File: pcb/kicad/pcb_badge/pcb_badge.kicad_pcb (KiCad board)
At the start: 2 copper layers, 82 x 132 mm, 249 parts, among them J1 DEALON USB-TYPE-C-018, J2 Conn_01x02_Pin, J3 Conn_01x04_Pin, J4 Conn_01x03_Pin, J5 Conn_01x03_Pin, J7 Conn_01x02_Pin, Q1 SI2302, Q2 JSM2301S, Q9 2N7002, Q90 2N7002, Q91 2N7002, Q910 2N7002, Q911 2N7002, Q912 2N7002, Q913 2N7002, Q914 2N7002, Q915 2N7002, Q92 2N7002, Q93 2N7002, Q94 2N7002, Q95 2N7002, Q96 2N7002, Q97 2N7002, Q98 2N7002, Q99 2N7002, SW1 SW_MEC_5E, SW2 SW_MEC_5E, SW3 SW_MEC_5E, SW4 SW_MEC_5E, SW5 SW_MEC_5E, SW6 SW_MEC_5E, SW7 SW_MEC_5E, SW8 SW_MEC_5E, U1 TLV70328DBVR, U2 QX2304L33F, U3 STM32F103CBT6, U4 74HC238, U6 IRM-H638T/TR2, U8 74HC238, Y1 TAXM8M4RFDCET2T

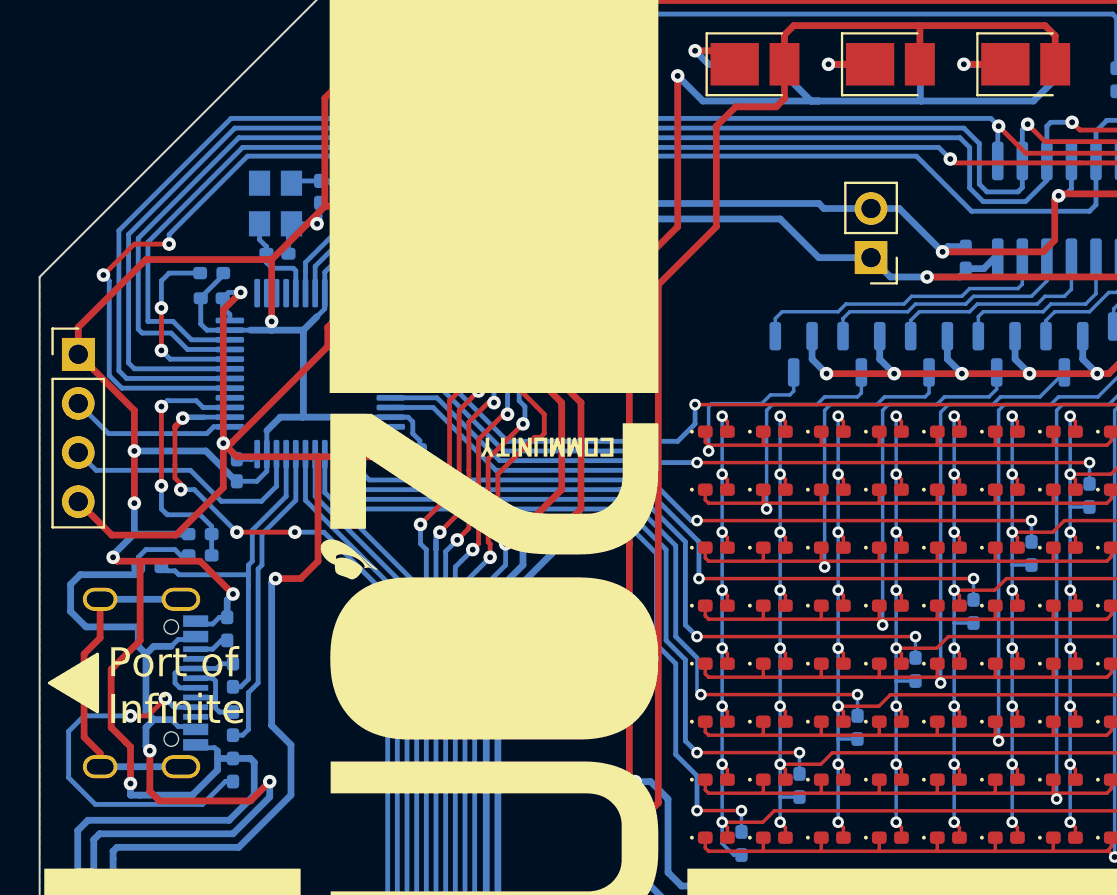
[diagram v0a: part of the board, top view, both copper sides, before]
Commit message: add accelerometer
1. change LedA1, A0 pin connection
2. add I2C1, U5 LSM6DS3TR-C
3. disconnect USB_DET
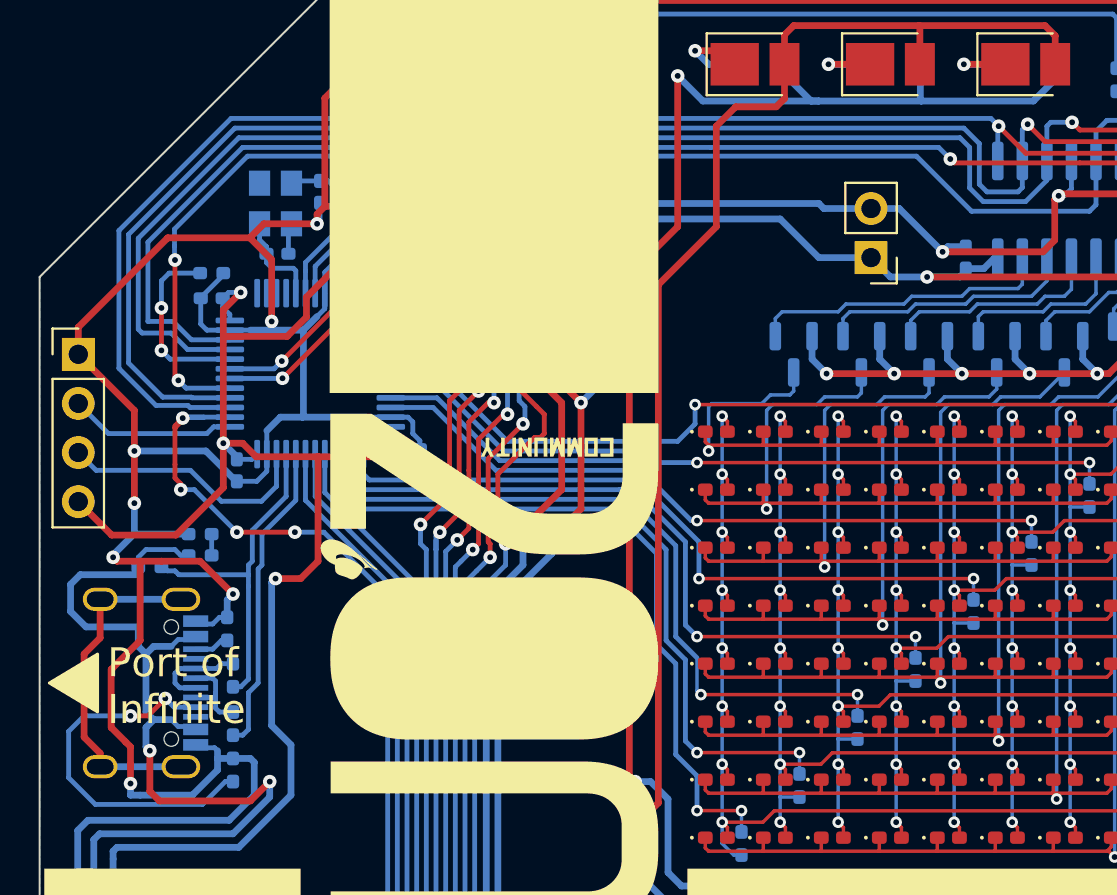
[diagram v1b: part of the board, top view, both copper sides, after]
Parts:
- added C50: 0.1u, Capacitor_SMD:C_0402_1005Metric_Pad0.74x0.62mm_HandSolder, B.Cu at (105.1, 45.8)
- added C51: 0.1u, Capacitor_SMD:C_0402_1005Metric_Pad0.74x0.62mm_HandSolder, B.Cu at (103.2, 49.2)
- added R50: 4.7k, Resistor_SMD:R_0402_1005Metric_Pad0.72x0.64mm_HandSolder, B.Cu at (99.9, 44.0)
- added R51: 4.7k, Resistor_SMD:R_0402_1005Metric_Pad0.72x0.64mm_HandSolder, B.Cu at (99.9, 46.8)
- added U5: LSM6DS3TR-C, myLib:QFN_S3TR-C_STM, B.Cu at (102.4, 46.2)
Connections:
- U3 pad 39: /MCU/USB_DET -> /LED Matrix/A0
- U3 pad 40: unconnected-(U3-PB4-Pad40) -> /LED Matrix/A1
- U3 pad 42: /LED Matrix/A0 -> /MCU/I2C1_SCL
- U3 pad 43: /LED Matrix/A1 -> /MCU/I2C1_SDA
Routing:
- net /MCU/I2C1_SDA: track 0.00 -> 20.6 mm, vias 0 -> 2
- net /MCU/I2C1_SCL: track 0.00 -> 19.9 mm, vias 0 -> 2
- net GND: track 883.9 -> 898.6 mm, vias 41 -> 42
- net /MCU/USB_DET: track 13.6 -> 1.10 mm, vias 2 -> 0
- net VCC: track 657.3 -> 664.7 mm, vias 20 -> 22
- net /LED Matrix/DEC_EN: track 84.9 -> 78.9 mm
- net /MCU/NOISE_IN: track 27.0 -> 28.0 mm
- net /MCU/PA3: track 52.3 -> 52.9 mm
- net /LED Matrix/A1: track 84.8 -> 85.4 mm
- net /LED Matrix/A0: track 83.2 -> 83.7 mm
